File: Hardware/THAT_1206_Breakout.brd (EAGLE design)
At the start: 44.5 x 20.3 mm, 32 parts, among them IC1 THAT1206, J1 INPUT, J2 CHASSIS, J3 RN, J4 TN, J5 SN, J6 1x4

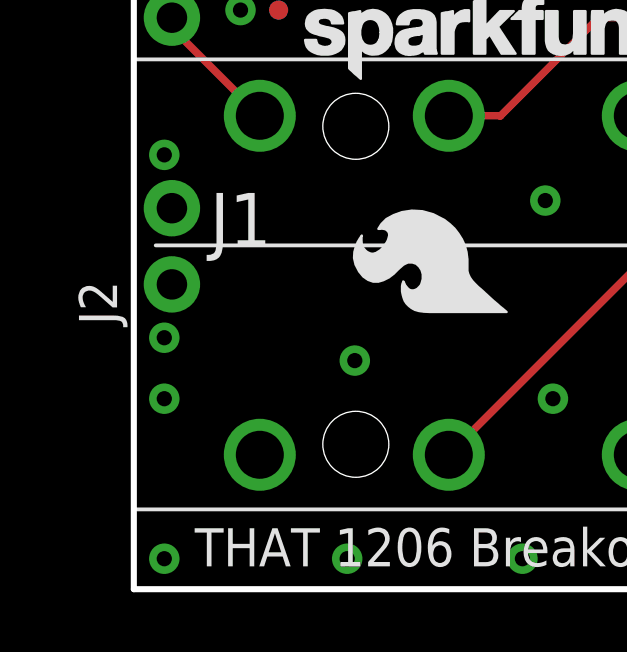
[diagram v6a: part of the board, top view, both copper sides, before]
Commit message: Fixing Kade's checklist issues.
-Un-"toed."
-Moved chassis ground connection.
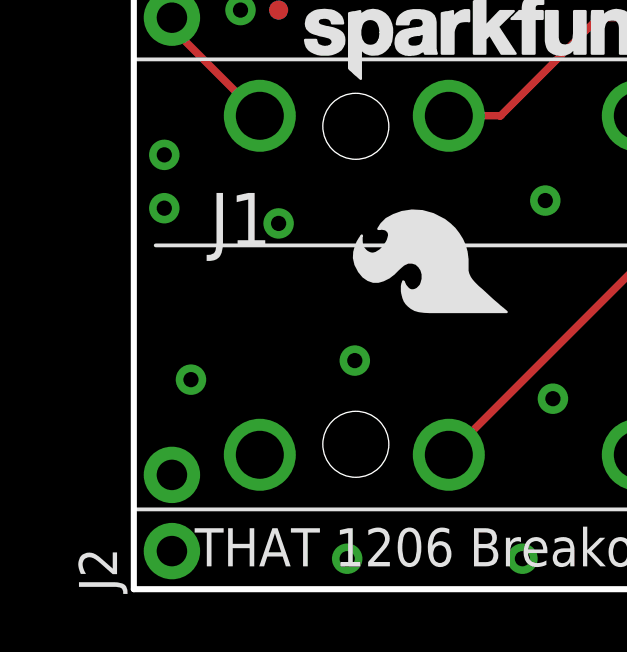
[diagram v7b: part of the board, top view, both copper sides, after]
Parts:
- moved J2 8.89 mm to (1.27, 1.27)
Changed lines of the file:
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@@
 <setting verticaltext="up"/>
 </settings>
-<grid distance="0.01" unitdist="inch" unit="inch" style="lines" multiple="1" display="yes" altdistance="0.005" altunitdist="inch" altunit="inch"/>
+<grid distance="0.05" unitdist="inch" unit="inch" style="lines" multiple="1" display="yes" altdistance="0.005" altunitdist="inch" altunit="inch"/>
 <layers>
-<layer number="1" name="Top" color="4" fill="1" visible="no" active="yes"/>
+<layer number="1" name="Top" color="4" fill="1" visible="yes" active="yes"/>
 <layer number="2" name="Route2" color="1" fill="3" visible="no" active="no"/>
 <layer number="3" name="Route3" color="4" fill="3" visible="no" active="no"/>
@@
 <layer number="14" name="Route14" color="1" fill="6" visible="no" active="no"/>
 <layer number="15" name="Route15" color="4" fill="6" visible="no" active="no"/>
-<layer number="16" name="Bottom" color="1" fill="1" visible="no" active="yes"/>
+<layer number="16" name="Bottom" color="1" fill="1" visible="yes" active="yes"/>
 <layer number="17" name="Pads" color="2" fill="1" visible="yes" active="yes"/>
 <layer number="18" name="Vias" color="2" fill="1" visible="yes" active="yes"/>
@@
 <layer number="37" name="tTest" color="7" fill="1" visible="no" active="yes"/>
 <layer number="38" name="bTest" color="7" fill="1" visible="no" active="yes"/>
-<layer number="39" name="tKeepout" color="4" fill="11" visible="yes" active="yes"/>
-<layer number="40" name="bKeepout" color="1" fill="11" visible="yes" active="yes"/>
-<layer number="41" name="tRestrict" color="4" fill="10" visible="yes" active="yes"/>
+<layer number="39" name="tKeepout" color="4" fill="11" visible="no" active="yes"/>
+<layer number="40" name="bKeepout" color="1" fill="11" visible="no" active="yes"/>
+<layer number="41" name="tRestrict" color="4" fill="10" visible="no" active="yes"/>
 <layer number="42" name="bRestrict" color="1" fill="10" visible="no" active="yes"/>
 <layer number="43" name="vRestrict" color="2" fill="10" visible="no" active="yes"/>
@@
 <layer number="45" name="Holes" color="7" fill="1" visible="yes" active="yes"/>
 <layer number="46" name="Milling" color="3" fill="1" visible="no" active="yes"/>
-<layer number="47" name="Measures" color="7" fill="1" visible="yes" active="yes"/>
+<layer number="47" name="Measures" color="7" fill="1" visible="no" active="yes"/>
 <layer number="48" name="Document" color="7" fill="1" visible="no" active="yes"/>
 <layer number="49" name="Reference" color="7" fill="1" visible="no" active="yes"/>
@@
 Line Receiver
 Breakout</text>
-<text x="2.794" y="6.604" size="1.27" layer="22" font="vector" ratio="15" rot="MR90">Chassis</text>
+<text x="1.27" y="4.826" size="1.27" layer="22" font="vector" ratio="15" rot="MR90" align="center-left">Chassis</text>
 <text x="26.162" y="0.508" size="1.016" layer="22" font="vector" ratio="15" rot="MR0" align="bottom-right">Cut jumper to
 isolate chassis
@@
 <attribute name="PROD_ID" value="CAP-08604" x="40.64" y="2.54" size="1.778" layer="27" font="vector" ratio="15" display="off"/>
 </element>
-<element name="J2" library="SparkFun-Connectors" package="1X02_NO_SILK" value="CHASSIS" x="1.27" y="10.16" rot="R90"/>
+<element name="J2" library="SparkFun-Connectors" package="1X02_NO_SILK" value="CHASSIS" x="1.27" y="1.27" rot="R90"/>
 <element name="J6" library="SparkFun-Connectors" package="1X04_NO_SILK_ALL_ROUND" value="1x4" x="43.18" y="6.35" rot="R90">
 <attribute name="PROD_ID" value="CONN-09696" x="43.18" y="6.35" size="1.778" layer="27" font="vector" ratio="15" rot="R90" display="off"/>
@@
 <via x="3.556" y="19.304" extent="1-16" drill="0.508"/>
 <via x="7.366" y="7.62" extent="1-16" drill="0.508"/>
-<via x="1.016" y="6.35" extent="1-16" drill="0.508"/>
-<via x="1.016" y="1.016" extent="1-16" drill="0.508"/>
+<via x="1.016" y="12.7" extent="1-16" drill="0.508"/>
+<via x="1.905" y="6.985" extent="1-16" drill="0.508"/>
 <via x="7.112" y="1.016" extent="1-16" drill="0.508"/>
 <via x="12.954" y="1.016" extent="1-16" drill="0.508"/>
@@
 <via x="23.622" y="4.318" extent="1-16" drill="0.508"/>
 <via x="1.016" y="14.478" extent="1-16" drill="0.508"/>
-<via x="1.016" y="8.382" extent="1-16" drill="0.508"/>
+<via x="4.826" y="12.192" extent="1-16" drill="0.508"/>
 </signal>
 <signal name="RCV">

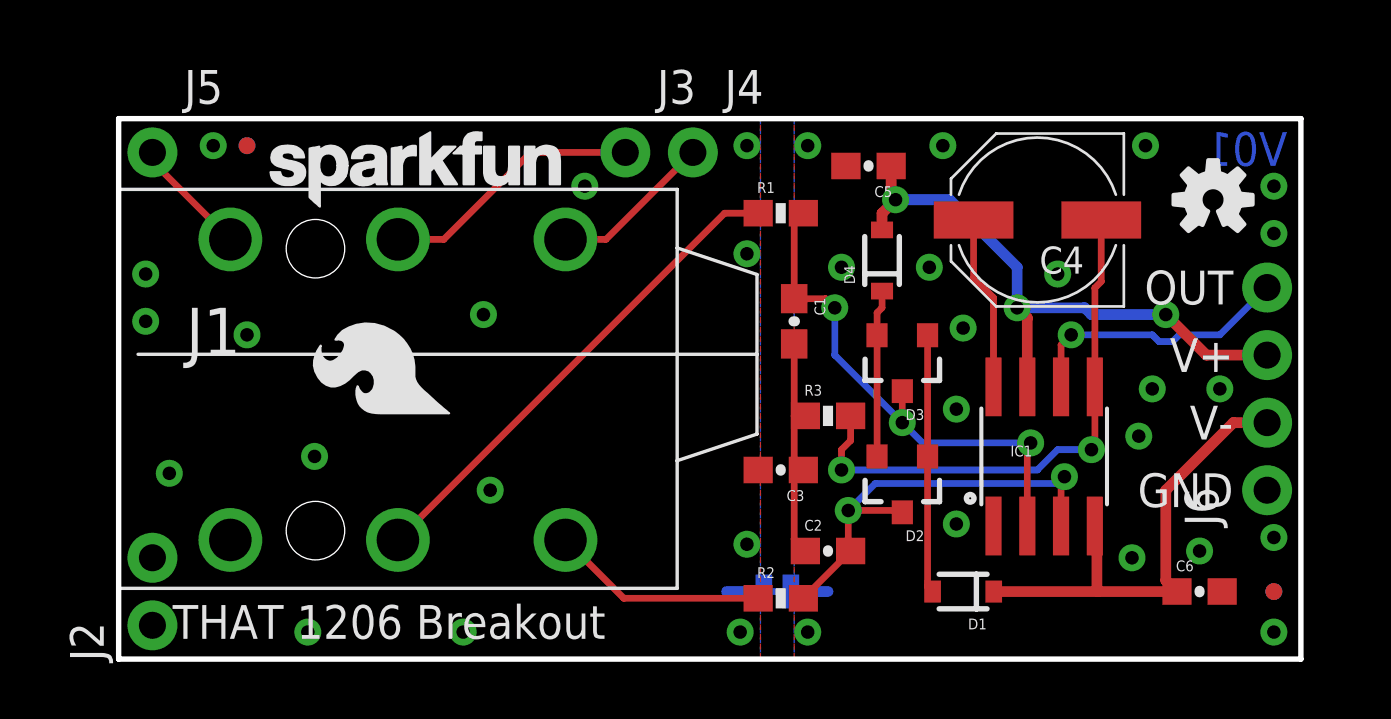
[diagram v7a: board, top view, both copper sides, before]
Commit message: Adding testpoints on T/R/S connections.
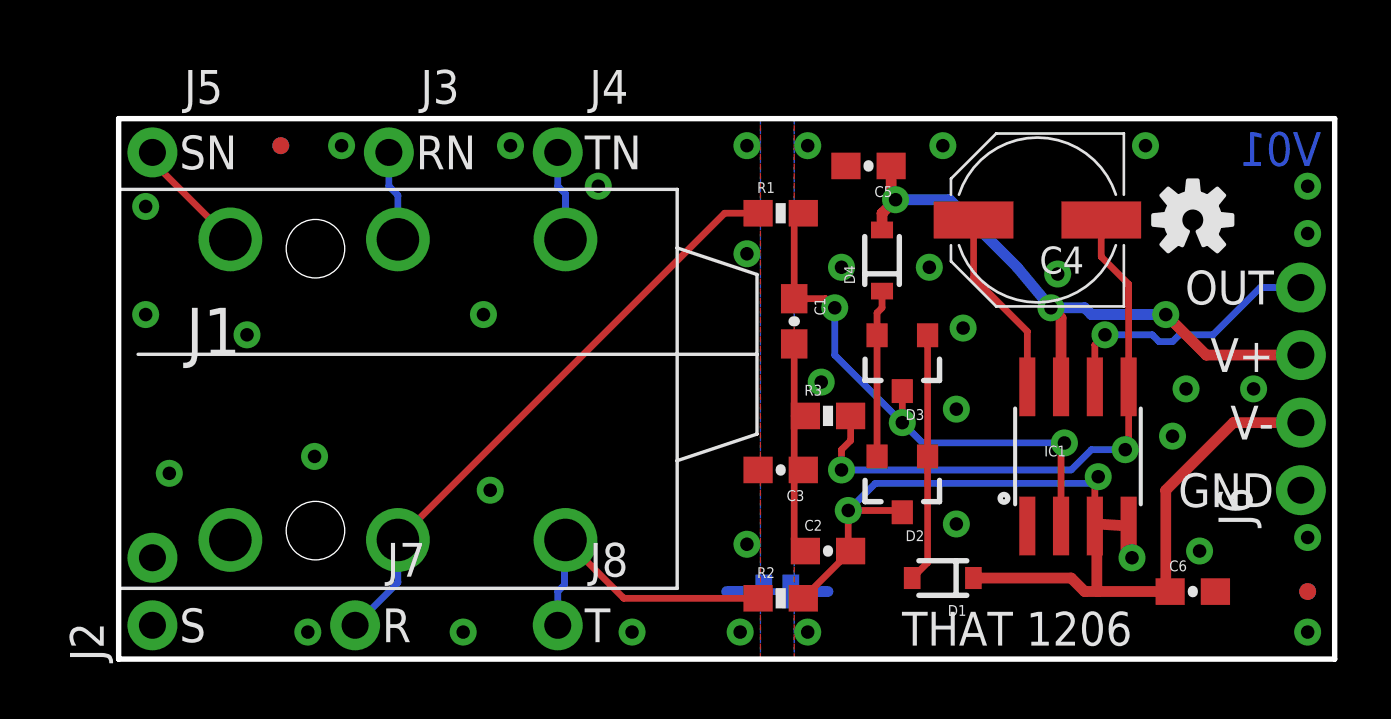
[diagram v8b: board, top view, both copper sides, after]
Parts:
- removed LOGO1: SFE_LOGO_FLAME.2_INCH, SparkFun-Aesthetics:SFE_LOGO_FLAME_.2
- removed LOGO5: SFE_LOGO_NAME.1_INCH, SparkFun-Aesthetics:SFE_LOGO_NAME_.1
- added J7: R, SparkFun-Connectors:1X01_NO_SILK
- added J8: T, SparkFun-Connectors:1X01_NO_SILK
- moved LOGO6 21.7 mm to (38.7, 14.0)
- moved J3 8.89 mm to (10.2, 19.1)
- moved J4 5.08 mm to (16.5, 19.1)
- moved LOGO3 3.64 mm to (40.4, 16.5)
- moved FD1 1.27 mm to (44.7, 2.54)
- moved FD4 1.27 mm to (44.7, 2.54)
- moved J6 1.27 mm to (44.5, 6.35)
- moved FD2 1.27 mm to (6.10, 19.3)
- moved FD3 1.27 mm to (6.10, 19.3)
- moved IC1 1.27 mm to (36.1, 7.62)
- moved LOGO4 1.08 mm to (40.4, 16.5)
- moved D1 0.92 mm to (31.0, 3.05)
- moved LOGO2 0.51 mm to (12.7, 12.2)
- moved C6 0.25 mm to (40.4, 2.54)
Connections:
- net N$1: now also J7.1
- net N$3: now also J8.1
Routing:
- net N$10: track 9.90 -> 3.41 mm
- net N$1: track 18.6 -> 22.5 mm
- net N$3: track 8.15 -> 11.5 mm
- net VNEG: track 18.4 -> 21.4 mm
- net N$9: track 6.14 -> 3.39 mm
- net N$6: track 20.7 -> 22.3 mm
- net N$2: track 20.6 -> 21.8 mm
- net N$4: track 16.7 -> 18.0 mm
- net N$7: track 6.58 -> 7.11 mm
- net GND-ISO: vias 15 -> 17
- net GND: vias 19 -> 20
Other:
- board size 44.5 x 20.3 mm -> 45.7 x 20.3 mm
- board text added: "R"
- board text added: "S"
- board text added: "T"
- board text added: "THAT 1206"
- board text removed: "THAT 1206 Breakout"
